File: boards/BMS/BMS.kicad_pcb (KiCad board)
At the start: 2 copper layers, 0 parts

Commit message: Progress
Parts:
- added C1: C_22uF, footprints:C_1206_OEM, F.Cu at (262.0, 74.2)
- added C10: C_0.1uF, footprints:C_0805_OEM, F.Cu at (229.6, 112.1)
- added C11: C_0.1uF, footprints:C_0805_OEM, F.Cu at (245.7, 94.8)
- added C12: 10nF, footprints:C_0805_OEM, F.Cu at (245.0, 110.7)
- added C13: 10nF, footprints:C_0805_OEM, F.Cu at (249.1, 105.4)
- added C2: C_0.1uF, footprints:C_0805_OEM, F.Cu at (283.5, 50.1)
- added C3: C_100pF, footprints:C_0805_OEM, F.Cu at (277.1, 50.1)
- added C4: C_0.1uF, footprints:C_0805_OEM, F.Cu at (265.8, 68.5)
- added C5: C_0.1uF, footprints:C_0805_OEM, F.Cu at (254.6, 79.7)
- added C6: C_47uF, footprints:C_0805_OEM, F.Cu at (292.1, 43.1)
- added C7: C_30pF, footprints:C_0805_OEM, F.Cu at (275.4, 60.9)
- added C8: C_30pF, footprints:C_0805_OEM, F.Cu at (289.5, 50.0)
- added C9: C_0.1uF, footprints:C_0805_OEM, F.Cu at (281.4, 55.3)
- added D1: LED_0805, footprints:LED_0805_OEM, F.Cu at (268.2, 62.0)
- added D2: LED_0805, footprints:LED_0805_OEM, F.Cu at (258.4, 68.5)
- added D3: D_Schottky_SOD123, footprints:D_SOD-123W_OEM, F.Cu at (239.6, 62.6)
- added D4: D_Zener_18V, footprints:DO-214AA, F.Cu at (149.9, 111.8)
- added D6: LED_0805, footprints:LED_0805_OEM, F.Cu at (240.8, 82.2)
- added D7: LED_0805, footprints:LED_0805_OEM, F.Cu at (274.0, 55.4)
- added D8: LED_0805, footprints:LED_0805_OEM, F.Cu at (254.8, 74.3)
- added D9: LED_0805, footprints:LED_0805_OEM, F.Cu at (153.7, 67.1)
- added F1: F_500mA_16V, footprints:Fuse_1210, F.Cu at (132.1, 110.5)
- added IC1: ATMEGA16M1, footprints:TQFP-32_7x7mm_Pitch0.8mm, F.Cu at (182.9, 80.0)
- added J1: Mounting_Hole_4-40, footprints:Mounting_Hole_4-40, F.Cu at (194.3, 116.8)
- added J2: Mounting_Hole_4-40, footprints:Mounting_Hole_4-40, F.Cu at (128.3, 66.0)
- added J3: Mounting_Hole_4-40, footprints:Mounting_Hole_4-40, F.Cu at (128.3, 115.6)
- added J4: Ultrafit_4, footprints:Ultrafit_4, F.Cu at (128.3, 100.3)
- added J5: Mounting_Hole_4-40, footprints:Mounting_Hole_4-40, F.Cu at (196.8, 66.0)
- added J6: Ultrafit_4, footprints:Ultrafit_4, F.Cu at (128.3, 78.7)
- added J7: NanoFit_2, footprints:Molex_NanoFit_1x02x2.50mm_Angled_OEM, F.Cu at (186.7, 109.2)
- added K1: G5Q-1A4-DC5-5V, footprints:Relay_SPST_OMRON-G5Q-1A4_OEM, F.Cu at (135.9, 83.8)
- added L1: L_4.7uH, footprints:4.7uH_Inductor_OEM, F.Cu at (139.7, 114.3)
- added P1: CONN_02X03, footprints:Pin_Header_Straight_2x03, F.Cu at (153.7, 99.1)
- added Q1: 2N7002, footprints:SOT-23F, F.Cu at (286.1, 44.1)
- added R1: R_1k, footprints:R_0805_OEM, F.Cu at (244.7, 68.4)
- added R10: R_10k, footprints:D_0805_OEM, F.Cu at (265.0, 79.7)
- added R15: R_200, footprints:R_0805_OEM, F.Cu at (271.4, 67.6)
- added R18: R_200, footprints:R_0805_OEM, F.Cu at (258.6, 85.2)
- added R19: R_200, footprints:R_0805_OEM, F.Cu at (294.8, 48.4)
- added R2: R_200, footprints:R_0805_OEM, F.Cu at (286.9, 55.4)
- added R20: R_100k, footprints:R_0805_OEM, F.Cu at (153.2, 72.8)
- added R21: R_100k, footprints:R_0805_OEM, F.Cu at (152.4, 78.1)
- added R22: 14.3k, footprints:R_0805_OEM, F.Cu at (160.2, 67.3)
- added R23: R_200, footprints:R_0805_OEM, F.Cu at (158.6, 72.8)
- added R24: 4.99k, footprints:R_0805_OEM, F.Cu at (240.8, 110.9)
- added R25: 3.01k, footprints:R_0805_OEM, F.Cu at (244.9, 105.5)
- added R26: R_1k, footprints:R_0805_OEM, F.Cu at (248.2, 100.2)
- added R27: 60.4, footprints:R_0805_OEM, F.Cu at (236.8, 110.6)
- added R28: 60.4, footprints:R_0805_OEM, F.Cu at (244.4, 100.2)
- added R3: R_200, footprints:R_0805_OEM, F.Cu at (280.7, 60.6)
- added R4: R_10k, footprints:R_0805_OEM, F.Cu at (253.7, 85.1)
- added R5: R_100, footprints:R_0805_OEM, F.Cu at (260.2, 79.9)
- added R6: R_10k, footprints:R_0805_OEM, F.Cu at (267.2, 73.9)
- added R7: R_55.1k, footprints:R_0805_OEM, F.Cu at (248.2, 82.2)
- added R9: R_200, footprints:R_0805_OEM, F.Cu at (276.3, 66.2)
- added T1: T_LAN_7490100111A, footprints:7490100111A, F.Cu at (170.2, 104.1)
- added U1: micro-match12pin, footprints:micromatch_female_ra_12, F.Cu at (180.3, 67.3)
- added U2: CAN_Transceiver, footprints:SOIC-8_3.9x4.9mm_Pitch1.27mm_OEM, F.Cu at (172.7, 73.7)
- added U3: TPS561201, footprints:SOT-23-6_OEM, F.Cu at (137.2, 106.7)
- added U4: SN74LVC1G17, footprints:SOT-23-5_OEM, F.Cu at (172.7, 82.5)
- added U5: AD623, footprints:AD623_SOIC-8, F.Cu at (138.4, 78.7)
- added U6: MCP6001, footprints:SOT-23-5_OEM, F.Cu at (146.0, 77.8)
- added U7: LTC6820, footprints:LTC6820_OEM, F.Cu at (182.9, 96.5)
- added Y1: Crystal_SMD, footprints:Crystal_SMD_FA238, F.Cu at (188.0, 86.4)

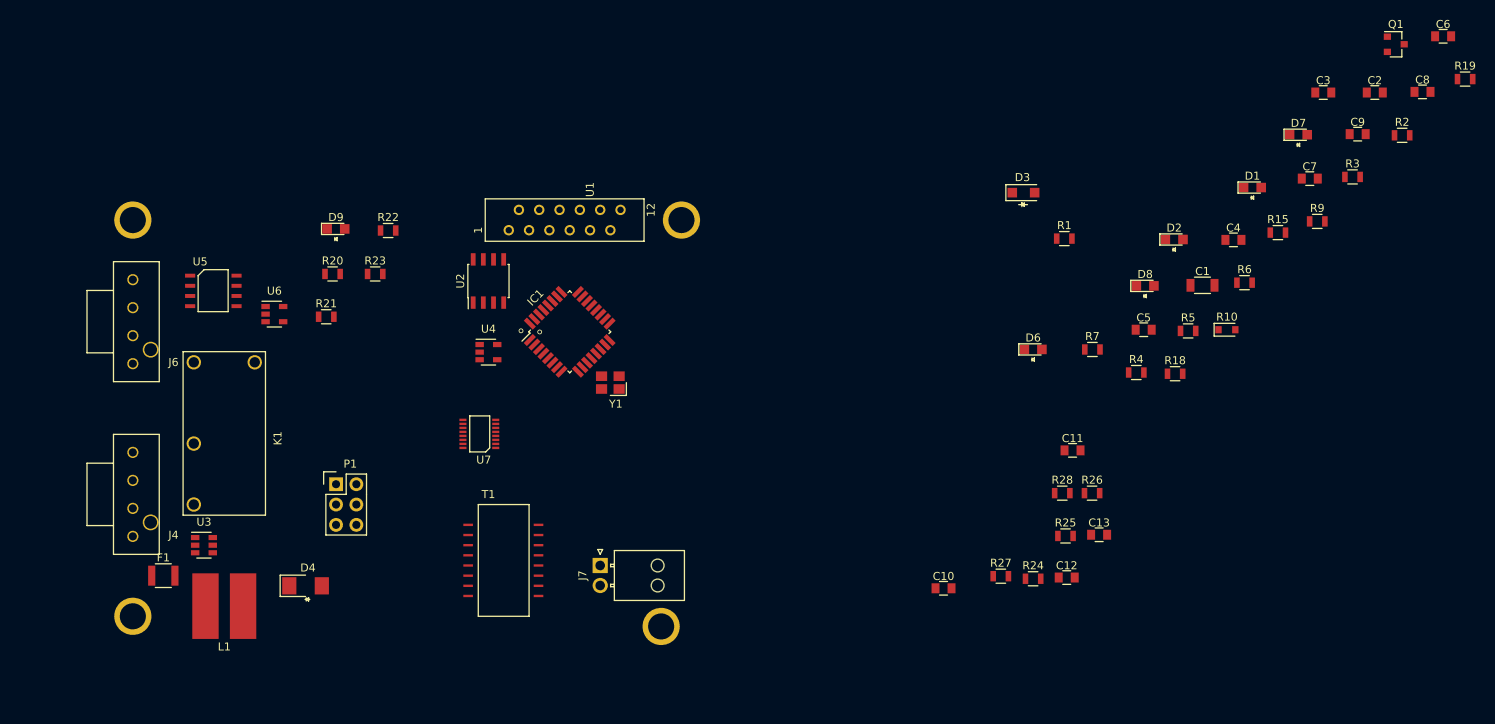
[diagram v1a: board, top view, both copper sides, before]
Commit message: BMS: updating files
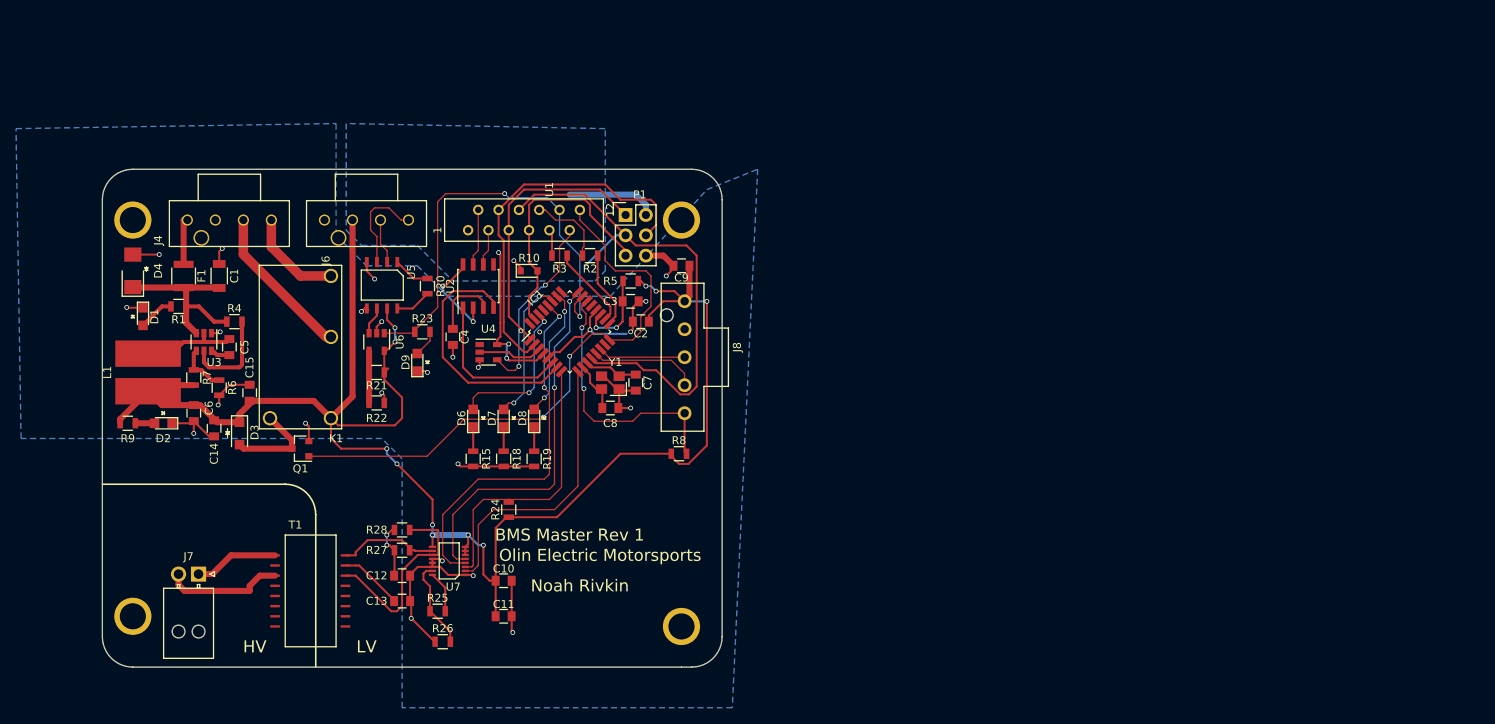
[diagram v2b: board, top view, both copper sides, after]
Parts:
- added C14: C_10uF_16V, footprints:C_0805_OEM, F.Cu at (138.4, 92.1)
- added C15: C_0.1uF, footprints:C_0805_OEM, F.Cu at (142.9, 87.6)
- added J8: Ultrafit_5, footprints:UltraFit_5, F.Cu at (194.3, 83.2)
- added R8: R_10k, footprints:R_0805_OEM, F.Cu at (196.5, 95.2)
- moved C6 163.1 mm to (135.9, 90.2), turned to 270 degrees
- moved R9 150.8 mm to (127.6, 91.4)
- moved Q1 145.9 mm to (149.2, 94.6), turned to 180 degrees
- moved D1 139.6 mm to (129.5, 78.1), turned to 270 degrees
- moved R6 128.8 mm to (139.1, 87.0), turned to 270 degrees
- moved D2 128.4 mm to (132.1, 91.4), turned to 180 degrees
- moved R19 125.7 mm to (178.4, 95.9), turned to 270 degrees
- moved C1 122.9 mm to (139.1, 73.0), turned to 90 degrees
- moved C5 114.3 mm to (140.3, 81.9), turned to 90 degrees
- moved R4 112.9 mm to (141.0, 78.7)
- moved R7 112.4 mm to (135.9, 85.7), turned to 270 degrees
- moved R1 111.0 mm to (134.0, 76.8), turned to 180 degrees
- moved C8 108.9 mm to (188.0, 89.5)
- moved D7 105.5 mm to (174.6, 90.8), turned to 90 degrees
- moved R15 104.5 mm to (170.8, 95.9), turned to 270 degrees
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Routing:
- net VCC: track 0.00 -> 252.0 mm, vias 0 -> 15
- net GND: track 0.00 -> 118.0 mm, vias 0 -> 26
- net Shutdown_Control: track 0.00 -> 72.8 mm, vias 0 -> 2
- net SCK: track 0.00 -> 64.7 mm
- net BSPD_Current_Sense: track 0.00 -> 55.4 mm, vias 0 -> 2
- net MOSI: track 0.00 -> 47.2 mm
- net SCK_iso: track 0.00 -> 46.5 mm, vias 0 -> 2
- net CS_iso: track 0.00 -> 46.3 mm, vias 0 -> 2
- net MOSI_iso: track 0.00 -> 35.8 mm
- net MISO_iso: track 0.00 -> 35.0 mm
- net MISO: track 0.00 -> 34.7 mm
- net Net-(IC1-Pad22): track 0.00 -> 33.2 mm, vias 0 -> 2
- net RESET: track 0.00 -> 31.8 mm
- net RXCAN: track 0.00 -> 31.6 mm
- net Net-(R28-Pad2): track 0.00 -> 25.9 mm
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- added copper zone on B.Cu, net GND
- added copper zone on B.Cu, net VCC
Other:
- board outline added: 77.5 x 62.2 mm
- board text added: "BMS Master Rev 1"
- board text added: "HV"
- board text added: "LV"
- board text added: "Noah Rivkin"
- board text added: "Olin Electric Motorsports"

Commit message: Revert "testing"
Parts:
- removed C14: C_10uF_16V, footprints:C_0805_OEM
- removed C15: C_0.1uF, footprints:C_0805_OEM
- removed J8: Ultrafit_5, footprints:UltraFit_5
- removed R8: R_10k, footprints:R_0805_OEM
- moved C6 163.1 mm to (292.1, 43.1), turned to 0 degrees
- moved R9 150.8 mm to (276.3, 66.2)
- moved Q1 145.9 mm to (286.1, 44.1), turned to 0 degrees
- moved D1 139.6 mm to (268.2, 62.0), turned to 0 degrees
- moved R6 128.8 mm to (267.2, 73.9), turned to 0 degrees
- moved D2 128.4 mm to (258.4, 68.5), turned to 0 degrees
- moved R19 125.7 mm to (294.8, 48.4), turned to 0 degrees
- moved C1 122.9 mm to (262.0, 74.2), turned to 0 degrees
- moved C5 114.3 mm to (254.6, 79.7), turned to 0 degrees
- moved R4 112.9 mm to (253.7, 85.1)
- moved R7 112.4 mm to (248.2, 82.2), turned to 0 degrees
- moved R1 111.0 mm to (244.7, 68.4), turned to 0 degrees
- moved C8 108.9 mm to (289.5, 50.0)
- moved D7 105.5 mm to (274.0, 55.4), turned to 0 degrees
- moved R15 104.5 mm to (271.4, 67.6), turned to 0 degrees
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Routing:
- net VCC: track 252.0 -> 0.00 mm, vias 15 -> 0
- net GND: track 118.0 -> 0.00 mm, vias 26 -> 0
- net Shutdown_Control: track 72.8 -> 0.00 mm, vias 2 -> 0
- net SCK: track 64.7 -> 0.00 mm
- net BSPD_Current_Sense: track 55.4 -> 0.00 mm, vias 2 -> 0
- net MOSI: track 47.2 -> 0.00 mm
- net SCK_iso: track 46.5 -> 0.00 mm, vias 2 -> 0
- net CS_iso: track 46.3 -> 0.00 mm, vias 2 -> 0
- net MOSI_iso: track 35.8 -> 0.00 mm
- net MISO_iso: track 35.0 -> 0.00 mm
- net MISO: track 34.7 -> 0.00 mm
- net Net-(IC1-Pad22): track 33.2 -> 0.00 mm, vias 2 -> 0
- net RESET: track 31.8 -> 0.00 mm
- net RXCAN: track 31.6 -> 0.00 mm
- net Net-(R28-Pad2): track 25.9 -> 0.00 mm
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- removed copper zone on B.Cu, net GND
- removed copper zone on B.Cu, net VCC
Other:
- board outline removed
- board text removed: "BMS Master Rev 1"
- board text removed: "HV"
- board text removed: "LV"
- board text removed: "Noah Rivkin"
- board text removed: "Olin Electric Motorsports"

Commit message: preparng for merge
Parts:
- added J8: Ultrafit_5, footprints:UltraFit_5, F.Cu at (201.9, 83.2)
- moved J4 3.18 mm to (126.4, 97.8)
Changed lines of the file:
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@@
 (kicad_pcb (version 4) (host pcbnew 4.0.7-e2-6376~58~ubuntu14.04.1)
   (general
-    (links 144)
-    (no_connects 144)
+    (links 149)
+    (no_connects 149)
     (area 0 0 0 0)
     (thickness 1.6)
@@
     (tracks 0)
     (zones 0)
-    (modules 64)
+    (modules 65)
     (nets 76)
   )
@@
     (pad 1 thru_hole circle (at 0 0) (size 4.6482 4.6482) (drill 3.2639) (layers *.Cu *.Mask))
   )
-  (module footprints:Ultrafit_4 (layer F.Cu)
-    (at 128.27 100.33)
-    (fp_text reference J4 (at 5.08 5.08) (layer F.SilkS)
-      (effects (font (size 1 1) (thickness 0.15)))
-    )
-    (fp_text value Ultrafit_4 (at 4.572 0.508 90) (layer F.Fab) hide
-      (effects (font (size 1 1) (thickness 0.15)))
-    )
-    (fp_line (start -5.588 -3.81) (end -2.54 -3.81) (layer F.Fab) (width 0.15))
-    (fp_line (start -2.54 -3.81) (end -2.54 3.81) (layer F.Fab) (width 0.15))
-    (fp_line (start -2.54 3.81) (end -5.588 3.81) (layer F.Fab) (width 0.15))
-    (fp_line (start -5.588 3.81) (end -5.588 -3.81) (layer F.Fab) (width 0.15))
-    (fp_text user "6.55mm Clearance" (at -4.07 0 90) (layer F.Fab)
-      (effects (font (size 0.5 0.5) (thickness 0.08)))
-    )
-    (fp_line (start -2.42 -3.9) (end -5.73 -3.9) (layer F.SilkS) (width 0.15))
-    (fp_line (start -5.73 -3.9) (end -5.73 3.9) (layer F.SilkS) (width 0.15))
-    (fp_line (start -5.73 3.9) (end -2.42 3.9) (layer F.SilkS) (width 0.15))
-    (fp_line (start -2.42 7.5) (end 3.302 7.5) (layer F.SilkS) (width 0.15))
-    (fp_line (start -2.42 -7.5) (end 3.302 -7.5) (layer F.SilkS) (width 0.15))
-    (fp_line (start -2.42 7.5) (end -2.42 -7.5) (layer F.SilkS) (width 0.15))
-    (fp_line (start 3.302 7.5) (end 3.302 -7.5) (layer F.SilkS) (width 0.15))
-    (pad 2 thru_hole circle (at 0 1.75) (size 1.397 1.397) (drill 1.02) (layers *.Cu *.Mask)
-      (net 2 GND))
-    (pad 1 thru_hole circle (at 0 5.25) (size 1.397 1.397) (drill 1.02) (layers *.Cu *.Mask)
-      (net 22 +12V))
-    (pad "" thru_hole circle (at 2.23 3.5) (size 1.981 1.981) (drill 1.6) (layers *.Cu *.Mask))
-    (pad 3 thru_hole circle (at 0 -1.75 180) (size 1.397 1.397) (drill 1.02) (layers *.Cu *.Mask)
-      (net 46 "Net-(J4-Pad3)"))
-    (pad 4 thru_hole circle (at 0 -5.25 180) (size 1.397 1.397) (drill 1.02) (layers *.Cu *.Mask)
-      (net 47 "Net-(J4-Pad4)"))
-  )
   (module footprints:Mounting_Hole_4-40 (layer F.Cu)
     (at 196.85 66.04)
@@
       (net 61 "Net-(R27-Pad1)"))
   )
+  (module footprints:Ultrafit_4 (layer F.Cu)
+    (at 126.365 97.79)
+    (fp_text reference J4 (at 5.08 5.08) (layer F.SilkS)
+      (effects (font (size 1 1) (thickness 0.15)))
+    )
+    (fp_text value Ultrafit_4 (at 4.572 0.508 90) (layer F.Fab) hide
+      (effects (font (size 1 1) (thickness 0.15)))
+    )
+    (fp_line (start -5.588 -3.81) (end -2.54 -3.81) (layer F.Fab) (width 0.15))
+    (fp_line (start -2.54 -3.81) (end -2.54 3.81) (layer F.Fab) (width 0.15))
+    (fp_line (start -2.54 3.81) (end -5.588 3.81) (layer F.Fab) (width 0.15))
+    (fp_line (start -5.588 3.81) (end -5.588 -3.81) (layer F.Fab) (width 0.15))
+    (fp_text user "6.55mm Clearance" (at -4.07 0 90) (layer F.Fab)
+      (effects (font (size 0.5 0.5) (thickness 0.08)))
+    )
+    (fp_line (start -2.42 -3.9) (end -5.73 -3.9) (layer F.SilkS) (width 0.15))
+    (fp_line (start -5.73 -3.9) (end -5.73 3.9) (layer F.SilkS) (width 0.15))
+    (fp_line (start -5.73 3.9) (end -2.42 3.9) (layer F.SilkS) (width 0.15))
+    (fp_line (start -2.42 7.5) (end 3.302 7.5) (layer F.SilkS) (width 0.15))
+    (fp_line (start -2.42 -7.5) (end 3.302 -7.5) (layer F.SilkS) (width 0.15))
+    (fp_line (start -2.42 7.5) (end -2.42 -7.5) (layer F.SilkS) (width 0.15))
+    (fp_line (start 3.302 7.5) (end 3.302 -7.5) (layer F.SilkS) (width 0.15))
+    (pad 2 thru_hole circle (at 0 1.75) (size 1.397 1.397) (drill 1.02) (layers *.Cu *.Mask)
+      (net 2 GND))
+    (pad 1 thru_hole circle (at 0 5.25) (size 1.397 1.397) (drill 1.02) (layers *.Cu *.Mask)
+      (net 22 +12V))
+    (pad "" thru_hole circle (at 2.23 3.5) (size 1.981 1.981) (drill 1.6) (layers *.Cu *.Mask))
+    (pad 3 thru_hole circle (at 0 -1.75 180) (size 1.397 1.397) (drill 1.02) (layers *.Cu *.Mask)
+      (net 46 "Net-(J4-Pad3)"))
+    (pad 4 thru_hole circle (at 0 -5.25 180) (size 1.397 1.397) (drill 1.02) (layers *.Cu *.Mask)
+      (net 47 "Net-(J4-Pad4)"))
+  )
+  (module footprints:UltraFit_5 (layer F.Cu)
+    (at 201.93 83.185 90)
+    (fp_text reference J8 (at -1.25 -9.5 270) (layer F.SilkS)
+      (effects (font (size 1 1) (thickness 0.15)))
+    )
+    (fp_text value Ultrafit_5 (at 0 1.5 90) (layer F.Fab)
+      (effects (font (size 1 1) (thickness 0.15)))
+    )
+    (fp_line (start 3.645 -8.41) (end -3.645 -8.41) (layer F.SilkS) (width 0.15))
+    (fp_line (start -3.645 -5.35) (end -3.645 -8.41) (layer F.SilkS) (width 0.15))
+    (fp_line (start 3.645 -5.35) (end 3.645 -8.41) (layer F.SilkS) (width 0.15))
+    (fp_line (start -9.25 -5.35) (end -3.645 -5.35) (layer F.SilkS) (width 0.15))
+    (fp_line (start 9.25 -5.35) (end 3.645 -5.35) (layer F.SilkS) (width 0.15))
+    (fp_line (start 9.25 0) (end 9.25 -5.35) (layer F.SilkS) (width 0.15))
+    (fp_line (start -9.25 0) (end -9.25 -5.35) (layer F.SilkS) (width 0.15))
+    (fp_line (start 0 0) (end -9.25 0) (layer F.SilkS) (width 0.15))
+    (fp_line (start 0 0) (end 9.25 0) (layer F.SilkS) (width 0.15))
+    (pad 1 thru_hole circle (at -7 -2.93 90) (size 1.724 1.724) (drill 1.06) (layers *.Cu *.Mask)
+      (net 3 VCC))
+    (pad 2 thru_hole circle (at -3.5 -2.93 90) (size 1.724 1.724) (drill 1.06) (layers *.Cu *.Mask)
+      (net 2 GND))
+    (pad 3 thru_hole circle (at 0 -2.93 90) (size 1.724 1.724) (drill 1.06) (layers *.Cu *.Mask)
+      (net 32 "Net-(IC1-Pad14)"))
+    (pad 4 thru_hole circle (at 3.5 -2.93 90) (size 1.724 1.724) (drill 1.06) (layers *.Cu *.Mask)
+      (net 31 "Net-(IC1-Pad13)"))
+    (pad 5 thru_hole circle (at 7 -2.93 90) (size 1.724 1.724) (drill 1.06) (layers *.Cu *.Mask)
+      (net 38 "Net-(IC1-Pad22)"))
+    (pad "" np_thru_hole circle (at -5.25 -0.7 90) (size 1.6 1.6) (drill 1.6) (layers *.Cu *.Mask))
+  )
 )
